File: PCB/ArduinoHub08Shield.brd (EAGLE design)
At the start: 57.1 x 53.3 mm, 2 parts

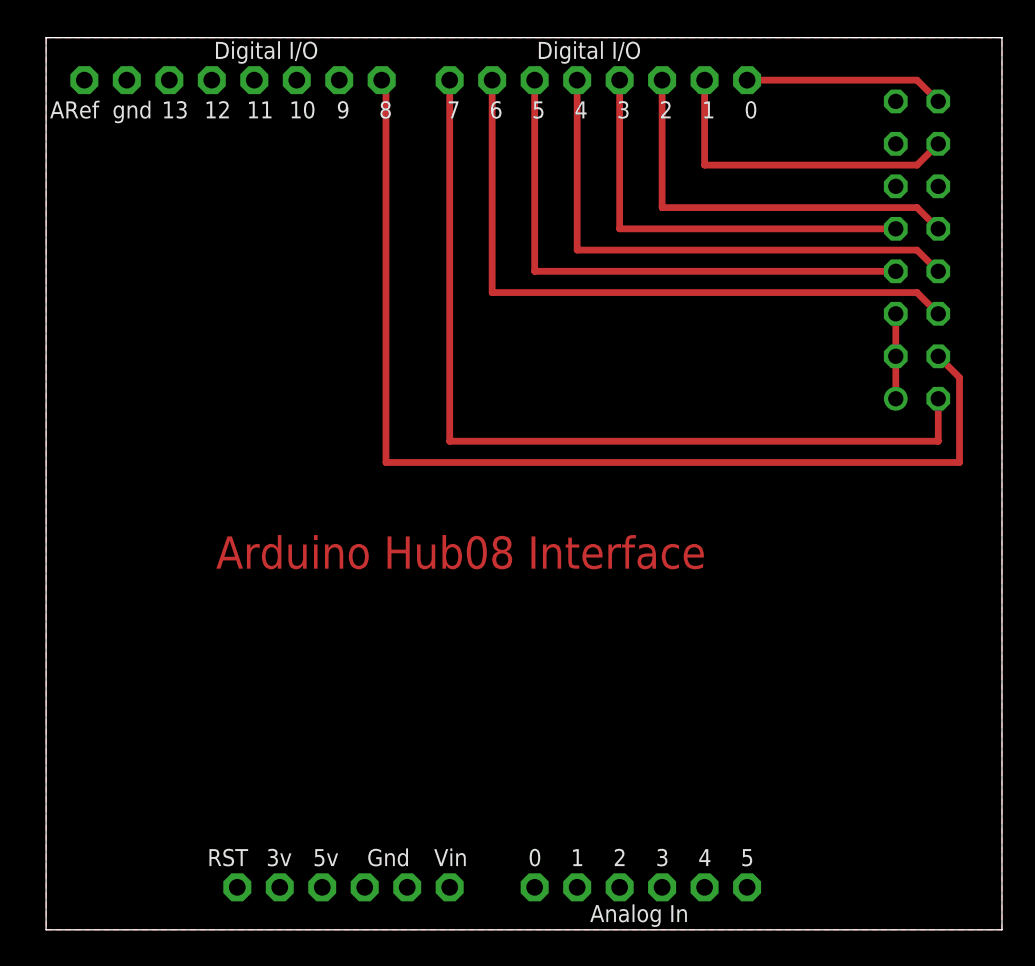
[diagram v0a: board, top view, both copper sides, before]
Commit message: Refactoring of the LCDDisplay library
because of the bad performance of the Ultrathin LED_Matrix
library (only about 25 frames/s refresh rate..) the complete
LEDDisplay Library has to be redesigned to talk directly to the
hardware in a more efficient way.
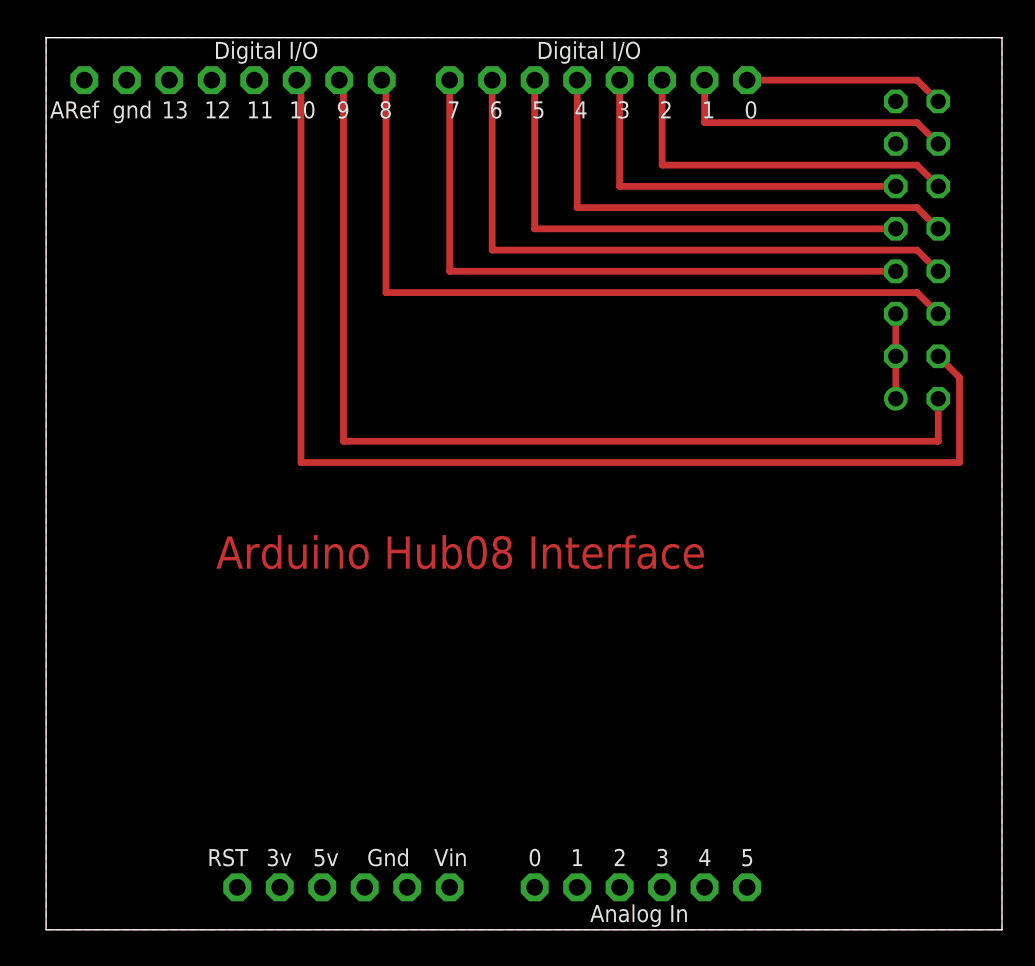
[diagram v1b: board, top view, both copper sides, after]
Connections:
- net SCK renamed S
- net STB renamed L
- removed net LA: CON1.2, U$1.D7
- removed net LB: CON1.4, U$1.D8
- removed net LC: CON1.6, U$1.D6
- removed net LD: CON1.8, U$1.D4
- new net A: CON1.2, U$1.D9
- new net B: CON1.4, U$1.D10
- new net C: CON1.6, U$1.D8
- new net D: CON1.8, U$1.D6
- net EN: now also U$1.D7; no longer U$1.D5
- net G1: now also U$1.D4; no longer U$1.D2
- net G2: now also U$1.D2
- net GND: no longer CON1.13, CON1.15
- net R1: now also U$1.D5; no longer U$1.D3
- net R2: now also U$1.D3
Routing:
- net B: track 0.00 -> 69.4 mm
- net LB: track 64.3 -> 0.00 mm
- net A: track 0.00 -> 59.9 mm
- net LA: track 53.3 -> 0.00 mm
- net C: track 0.00 -> 46.5 mm
- net LC: track 39.9 -> 0.00 mm
- net D: track 0.00 -> 37.4 mm
- net LD: track 32.3 -> 0.00 mm
- net R2: track 0.00 -> 22.9 mm
- net G2: track 0.00 -> 22.1 mm
- net R1: track 25.4 -> 30.5 mm
- net G1: track 24.7 -> 29.7 mm
- net EN: track 33.0 -> 38.1 mm
- net L: track 19.6 -> 17.0 mm
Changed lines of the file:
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@@
 <contactref element="CON1" pad="3"/>
 <contactref element="CON1" pad="5"/>
-<contactref element="CON1" pad="13"/>
-<contactref element="CON1" pad="15"/>
 <contactref element="U$1" pad="GND"/>
 <polygon width="0.3048" layer="1">
@@
 <signal name="R1">
 <contactref element="CON1" pad="9"/>
-<wire x1="72.39" y1="41.91" x2="55.88" y2="41.91" width="0.4064" layer="1"/>
-<contactref element="U$1" pad="D3"/>
-<wire x1="55.88" y1="41.91" x2="55.88" y2="50.8" width="0.4064" layer="1"/>
+<wire x1="72.39" y1="41.91" x2="50.8" y2="41.91" width="0.4064" layer="1"/>
+<contactref element="U$1" pad="D5"/>
+<wire x1="50.8" y1="50.8" x2="50.8" y2="41.91" width="0.4064" layer="1"/>
 </signal>
-<signal name="STB">
+<signal name="L">
 <contactref element="CON1" pad="14"/>
 <contactref element="U$1" pad="D1"/>
-<wire x1="74.93" y1="46.99" x2="73.66" y2="45.72" width="0.4064" layer="1"/>
-<wire x1="73.66" y1="45.72" x2="60.96" y2="45.72" width="0.4064" layer="1"/>
-<wire x1="60.96" y1="45.72" x2="60.96" y2="50.8" width="0.4064" layer="1"/>
+<wire x1="74.93" y1="46.99" x2="73.66" y2="48.26" width="0.4064" layer="1"/>
+<wire x1="73.66" y1="48.26" x2="60.96" y2="48.26" width="0.4064" layer="1"/>
+<wire x1="60.96" y1="48.26" x2="60.96" y2="50.8" width="0.4064" layer="1"/>
 </signal>
-<signal name="SCK">
+<signal name="S">
 <contactref element="CON1" pad="16"/>
 <contactref element="U$1" pad="D0"/>
@@
 <wire x1="73.66" y1="50.8" x2="63.5" y2="50.8" width="0.4064" layer="1"/>
 </signal>
-<signal name="LD">
+<signal name="D">
 <contactref element="CON1" pad="8"/>
 <wire x1="74.93" y1="39.37" x2="73.66" y2="40.64" width="0.4064" layer="1"/>
-<wire x1="73.66" y1="40.64" x2="53.34" y2="40.64" width="0.4064" layer="1"/>
-<contactref element="U$1" pad="D4"/>
-<wire x1="53.34" y1="40.64" x2="53.34" y2="50.8" width="0.4064" layer="1"/>
+<wire x1="73.66" y1="40.64" x2="48.26" y2="40.64" width="0.4064" layer="1"/>
+<contactref element="U$1" pad="D6"/>
+<wire x1="48.26" y1="50.8" x2="48.26" y2="40.64" width="0.4064" layer="1"/>
 </signal>
-<signal name="LC">
+<signal name="C">
 <contactref element="CON1" pad="6"/>
 <wire x1="74.93" y1="36.83" x2="73.66" y2="38.1" width="0.4064" layer="1"/>
-<wire x1="73.66" y1="38.1" x2="48.26" y2="38.1" width="0.4064" layer="1"/>
-<contactref element="U$1" pad="D6"/>
-<wire x1="48.26" y1="38.1" x2="48.26" y2="50.8" width="0.4064" layer="1"/>
+<wire x1="73.66" y1="38.1" x2="41.91" y2="38.1" width="0.4064" layer="1"/>
+<contactref element="U$1" pad="D8"/>
+<wire x1="41.656" y1="50.8" x2="41.91" y2="50.8" width="0.4064" layer="1"/>
+<wire x1="41.91" y1="50.8" x2="41.91" y2="38.1" width="0.4064" layer="1"/>
 </signal>
-<signal name="LB">
+<signal name="B">
 <contactref element="CON1" pad="4"/>
 <wire x1="74.93" y1="34.29" x2="76.2" y2="33.02" width="0.4064" layer="1"/>
 <wire x1="76.2" y1="33.02" x2="76.2" y2="27.94" width="0.4064" layer="1"/>
-<wire x1="76.2" y1="27.94" x2="41.91" y2="27.94" width="0.4064" layer="1"/>
-<contactref element="U$1" pad="D8"/>
-<wire x1="41.91" y1="27.94" x2="41.91" y2="50.8" width="0.4064" layer="1"/>
-<wire x1="41.91" y1="50.8" x2="41.656" y2="50.8" width="0.4064" layer="1"/>
+<wire x1="76.2" y1="27.94" x2="36.83" y2="27.94" width="0.4064" layer="1"/>
+<contactref element="U$1" pad="D10"/>
+<wire x1="36.576" y1="50.8" x2="36.83" y2="50.8" width="0.4064" layer="1"/>
+<wire x1="36.83" y1="50.8" x2="36.83" y2="27.94" width="0.4064" layer="1"/>
 </signal>
-<signal name="LA">
+<signal name="A">
 <contactref element="CON1" pad="2"/>
 <wire x1="74.93" y1="31.75" x2="74.93" y2="29.21" width="0.4064" layer="1"/>
-<wire x1="74.93" y1="29.21" x2="45.72" y2="29.21" width="0.4064" layer="1"/>
-<contactref element="U$1" pad="D7"/>
-<wire x1="45.72" y1="29.21" x2="45.72" y2="50.8" width="0.4064" layer="1"/>
+<wire x1="74.93" y1="29.21" x2="39.37" y2="29.21" width="0.4064" layer="1"/>
+<contactref element="U$1" pad="D9"/>
+<wire x1="39.116" y1="50.8" x2="39.37" y2="50.8" width="0.4064" layer="1"/>
+<wire x1="39.37" y1="50.8" x2="39.37" y2="29.21" width="0.4064" layer="1"/>
 </signal>
 <signal name="EN">
 <contactref element="CON1" pad="7"/>
-<wire x1="72.39" y1="39.37" x2="50.8" y2="39.37" width="0.4064" layer="1"/>
-<contactref element="U$1" pad="D5"/>
-<wire x1="50.8" y1="39.37" x2="50.8" y2="50.8" width="0.4064" layer="1"/>
+<wire x1="72.39" y1="39.37" x2="45.72" y2="39.37" width="0.4064" layer="1"/>
+<contactref element="U$1" pad="D7"/>
+<wire x1="45.72" y1="50.8" x2="45.72" y2="39.37" width="0.4064" layer="1"/>
 </signal>
 <signal name="G1">
 <contactref element="CON1" pad="10"/>
 <wire x1="74.93" y1="41.91" x2="73.66" y2="43.18" width="0.4064" layer="1"/>
-<wire x1="73.66" y1="43.18" x2="58.42" y2="43.18" width="0.4064" layer="1"/>
-<contactref element="U$1" pad="D2"/>
-<wire x1="58.42" y1="43.18" x2="58.42" y2="50.8" width="0.4064" layer="1"/>
+<wire x1="73.66" y1="43.18" x2="53.34" y2="43.18" width="0.4064" layer="1"/>
+<contactref element="U$1" pad="D4"/>
+<wire x1="53.34" y1="50.8" x2="53.34" y2="43.18" width="0.4064" layer="1"/>
 </signal>
 <signal name="R2">
 <contactref element="CON1" pad="11"/>
+<contactref element="U$1" pad="D3"/>
+<wire x1="72.39" y1="44.45" x2="55.88" y2="44.45" width="0.4064" layer="1"/>
+<wire x1="55.88" y1="44.45" x2="55.88" y2="50.8" width="0.4064" layer="1"/>
 </signal>
 <signal name="G2">
 <contactref element="CON1" pad="12"/>
+<contactref element="U$1" pad="D2"/>
+<wire x1="74.93" y1="44.45" x2="73.66" y2="45.72" width="0.4064" layer="1"/>
+<wire x1="73.66" y1="45.72" x2="58.42" y2="45.72" width="0.4064" layer="1"/>
+<wire x1="58.42" y1="45.72" x2="58.42" y2="50.8" width="0.4064" layer="1"/>
 </signal>
 </signals>

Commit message: isr refactored and fully implemented (tests pending..)
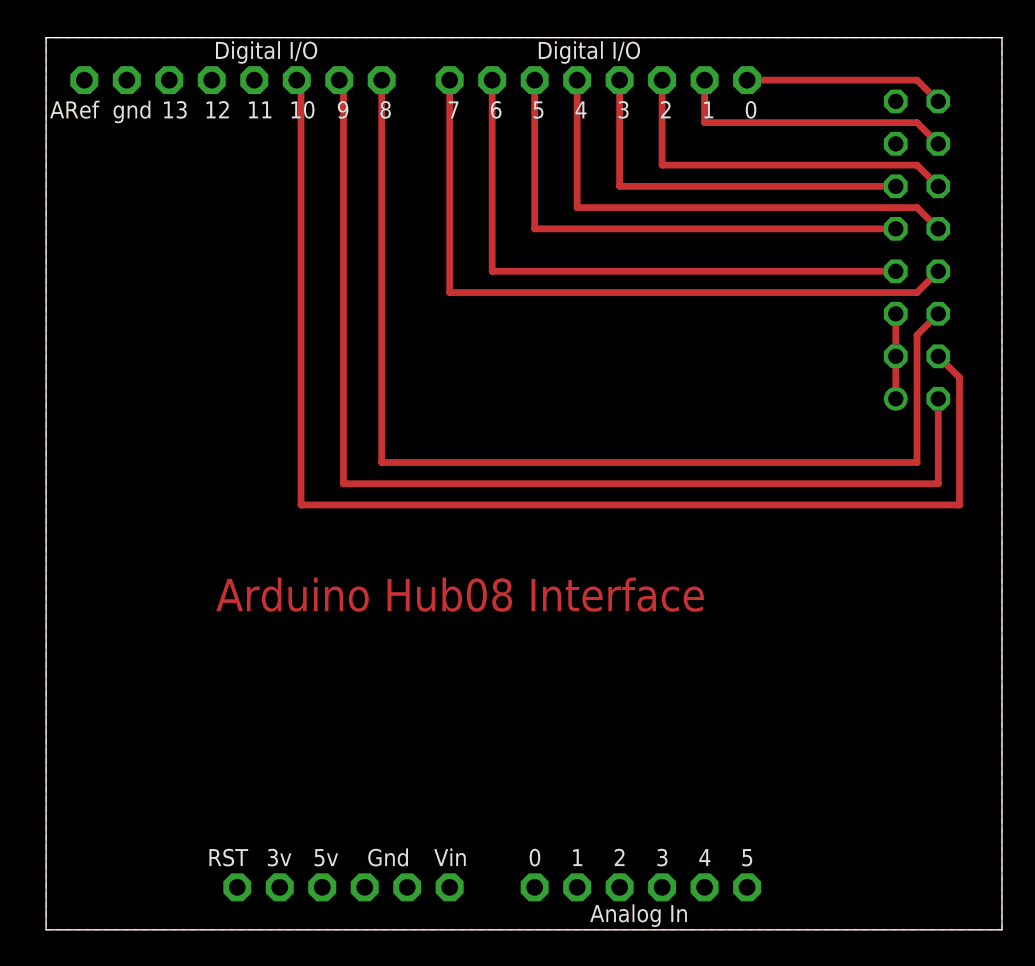
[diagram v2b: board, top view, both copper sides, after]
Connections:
- net D: now also U$1.D7; no longer U$1.D6
- net EN: now also U$1.D6; no longer U$1.D7
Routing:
- net C: track 46.5 -> 64.3 mm
- net B: track 69.4 -> 74.4 mm
- net A: track 59.9 -> 65.0 mm
- net D: track 37.4 -> 42.4 mm
- net EN: track 38.1 -> 35.6 mm
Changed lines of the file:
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@@
 <wire x1="78.74" y1="53.34" x2="78.74" y2="0" width="0" layer="20"/>
 <wire x1="78.74" y1="0" x2="21.59" y2="0" width="0" layer="20"/>
-<text x="31.75" y="21.59" size="1.9304" layer="1" font="vector" ratio="15">Arduino Hub08 Interface</text>
-<text x="31.75" y="19.05" size="1.9304" layer="1" font="vector" ratio="15" rot="R180" align="bottom-right">&gt;LAST_DATE_TIME</text>
+<text x="31.75" y="19.05" size="1.9304" layer="1" font="vector" ratio="15">Arduino Hub08 Interface</text>
+<text x="31.75" y="16.51" size="1.9304" layer="1" font="vector" ratio="15" rot="R180" align="bottom-right">&gt;LAST_DATE_TIME</text>
 </plain>
 <attributes>
@@
 <signal name="D">
 <contactref element="CON1" pad="8"/>
-<wire x1="74.93" y1="39.37" x2="73.66" y2="40.64" width="0.4064" layer="1"/>
-<wire x1="73.66" y1="40.64" x2="48.26" y2="40.64" width="0.4064" layer="1"/>
-<contactref element="U$1" pad="D6"/>
-<wire x1="48.26" y1="50.8" x2="48.26" y2="40.64" width="0.4064" layer="1"/>
+<contactref element="U$1" pad="D7"/>
+<wire x1="74.93" y1="39.37" x2="73.66" y2="38.1" width="0.4064" layer="1"/>
+<wire x1="73.66" y1="38.1" x2="45.72" y2="38.1" width="0.4064" layer="1"/>
+<wire x1="45.72" y1="38.1" x2="45.72" y2="50.8" width="0.4064" layer="1"/>
 </signal>
 <signal name="C">
 <contactref element="CON1" pad="6"/>
-<wire x1="74.93" y1="36.83" x2="73.66" y2="38.1" width="0.4064" layer="1"/>
-<wire x1="73.66" y1="38.1" x2="41.91" y2="38.1" width="0.4064" layer="1"/>
 <contactref element="U$1" pad="D8"/>
-<wire x1="41.656" y1="50.8" x2="41.91" y2="50.8" width="0.4064" layer="1"/>
-<wire x1="41.91" y1="50.8" x2="41.91" y2="38.1" width="0.4064" layer="1"/>
+<wire x1="74.93" y1="36.83" x2="73.66" y2="35.56" width="0.4064" layer="1"/>
+<wire x1="73.66" y1="35.56" x2="73.66" y2="27.94" width="0.4064" layer="1"/>
+<wire x1="73.66" y1="27.94" x2="41.656" y2="27.94" width="0.4064" layer="1"/>
+<wire x1="41.656" y1="27.94" x2="41.656" y2="50.8" width="0.4064" layer="1"/>
 </signal>
 <signal name="B">
 <contactref element="CON1" pad="4"/>
 <wire x1="74.93" y1="34.29" x2="76.2" y2="33.02" width="0.4064" layer="1"/>
-<wire x1="76.2" y1="33.02" x2="76.2" y2="27.94" width="0.4064" layer="1"/>
-<wire x1="76.2" y1="27.94" x2="36.83" y2="27.94" width="0.4064" layer="1"/>
+<wire x1="76.2" y1="33.02" x2="76.2" y2="25.4" width="0.4064" layer="1"/>
+<wire x1="76.2" y1="25.4" x2="36.83" y2="25.4" width="0.4064" layer="1"/>
 <contactref element="U$1" pad="D10"/>
 <wire x1="36.576" y1="50.8" x2="36.83" y2="50.8" width="0.4064" layer="1"/>
-<wire x1="36.83" y1="50.8" x2="36.83" y2="27.94" width="0.4064" layer="1"/>
+<wire x1="36.83" y1="50.8" x2="36.83" y2="25.4" width="0.4064" layer="1"/>
 </signal>
 <signal name="A">
 <contactref element="CON1" pad="2"/>
-<wire x1="74.93" y1="31.75" x2="74.93" y2="29.21" width="0.4064" layer="1"/>
-<wire x1="74.93" y1="29.21" x2="39.37" y2="29.21" width="0.4064" layer="1"/>
+<wire x1="74.93" y1="31.75" x2="74.93" y2="26.67" width="0.4064" layer="1"/>
+<wire x1="74.93" y1="26.67" x2="39.37" y2="26.67" width="0.4064" layer="1"/>
 <contactref element="U$1" pad="D9"/>
 <wire x1="39.116" y1="50.8" x2="39.37" y2="50.8" width="0.4064" layer="1"/>
-<wire x1="39.37" y1="50.8" x2="39.37" y2="29.21" width="0.4064" layer="1"/>
+<wire x1="39.37" y1="50.8" x2="39.37" y2="26.67" width="0.4064" layer="1"/>
 </signal>
 <signal name="EN">
 <contactref element="CON1" pad="7"/>
-<wire x1="72.39" y1="39.37" x2="45.72" y2="39.37" width="0.4064" layer="1"/>
-<contactref element="U$1" pad="D7"/>
-<wire x1="45.72" y1="50.8" x2="45.72" y2="39.37" width="0.4064" layer="1"/>
+<wire x1="72.39" y1="39.37" x2="48.26" y2="39.37" width="0.4064" layer="1"/>
+<contactref element="U$1" pad="D6"/>
+<wire x1="48.26" y1="39.37" x2="48.26" y2="50.8" width="0.4064" layer="1"/>
 </signal>
 <signal name="G1">

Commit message: another refactoring and code cleanups, see commit msg.
For performance reasons we constraint the usage of the
hardware ports to allow us to be more performant in the
inner loop of the ISR.

The schematic and PCM were changed to adapt these constraints.
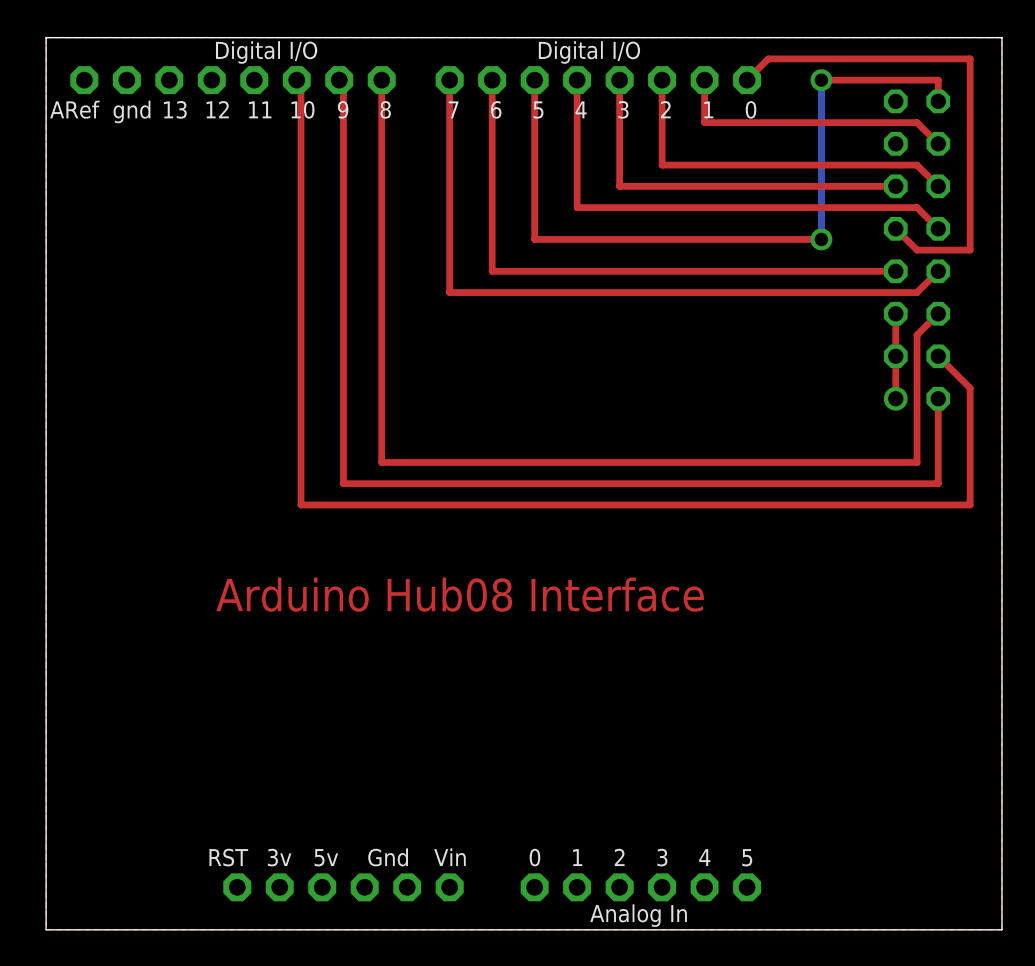
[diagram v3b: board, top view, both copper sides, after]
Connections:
- net R1: now also U$1.D0; no longer U$1.D5
- net S: now also U$1.D5; no longer U$1.D0
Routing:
- net S: track 12.0 -> 44.5 mm, vias 0 -> 2
- net B: track 74.4 -> 75.3 mm
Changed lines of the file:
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@@
 <param name="rlMinPadBottom" value="10mil"/>
 <param name="rlMaxPadBottom" value="20mil"/>
-<param name="rlMinViaOuter" value="8mil"/>
+<param name="rlMinViaOuter" value="10mil"/>
 <param name="rlMaxViaOuter" value="20mil"/>
 <param name="rlMinViaInner" value="8mil"/>
@@
 <signal name="R1">
 <contactref element="CON1" pad="9"/>
-<wire x1="72.39" y1="41.91" x2="50.8" y2="41.91" width="0.4064" layer="1"/>
-<contactref element="U$1" pad="D5"/>
-<wire x1="50.8" y1="50.8" x2="50.8" y2="41.91" width="0.4064" layer="1"/>
+<contactref element="U$1" pad="D0"/>
+<wire x1="72.39" y1="41.91" x2="73.66" y2="40.64" width="0.4064" layer="1"/>
+<wire x1="73.66" y1="40.64" x2="76.835" y2="40.64" width="0.4064" layer="1"/>
+<wire x1="76.835" y1="40.64" x2="76.835" y2="52.07" width="0.4064" layer="1"/>
+<wire x1="76.835" y1="52.07" x2="64.77" y2="52.07" width="0.4064" layer="1"/>
+<wire x1="64.77" y1="52.07" x2="63.5" y2="50.8" width="0.4064" layer="1"/>
 </signal>
 <signal name="L">
@@
 <signal name="S">
 <contactref element="CON1" pad="16"/>
-<contactref element="U$1" pad="D0"/>
-<wire x1="74.93" y1="49.53" x2="73.66" y2="50.8" width="0.4064" layer="1"/>
-<wire x1="73.66" y1="50.8" x2="63.5" y2="50.8" width="0.4064" layer="1"/>
+<contactref element="U$1" pad="D5"/>
+<wire x1="74.93" y1="49.53" x2="74.93" y2="50.8" width="0.4064" layer="1"/>
+<wire x1="74.93" y1="50.8" x2="67.945" y2="50.8" width="0.4064" layer="1"/>
+<via x="67.945" y="50.8" extent="1-16" drill="0.8" shape="square"/>
+<wire x1="67.945" y1="50.8" x2="67.945" y2="41.275" width="0.4064" layer="16"/>
+<via x="67.945" y="41.275" extent="1-16" drill="0.8" shape="square"/>
+<wire x1="67.945" y1="41.275" x2="50.8" y2="41.275" width="0.4064" layer="1"/>
+<wire x1="50.8" y1="41.275" x2="50.8" y2="50.8" width="0.4064" layer="1"/>
 </signal>
 <signal name="D">
@@
 <signal name="B">
 <contactref element="CON1" pad="4"/>
-<wire x1="74.93" y1="34.29" x2="76.2" y2="33.02" width="0.4064" layer="1"/>
-<wire x1="76.2" y1="33.02" x2="76.2" y2="25.4" width="0.4064" layer="1"/>
-<wire x1="76.2" y1="25.4" x2="36.83" y2="25.4" width="0.4064" layer="1"/>
+<wire x1="74.93" y1="34.29" x2="76.835" y2="32.385" width="0.4064" layer="1"/>
+<wire x1="76.835" y1="32.385" x2="76.835" y2="25.4" width="0.4064" layer="1"/>
+<wire x1="76.835" y1="25.4" x2="36.83" y2="25.4" width="0.4064" layer="1"/>
 <contactref element="U$1" pad="D10"/>
 <wire x1="36.576" y1="50.8" x2="36.83" y2="50.8" width="0.4064" layer="1"/>
